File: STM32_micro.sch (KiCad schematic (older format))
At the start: 61 parts

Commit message: asignacion pines de control
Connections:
- net labels added: FMC_A0, FMC_A1, FMC_A2, FMC_A3, FMC_A4, FMC_A5, FMC_A6, FMC_A7, FMC_A[7...0], FMC_D0, FMC_D1, FMC_D10, FMC_D11, FMC_D12, FMC_D13, FMC_D14, FMC_D15, FMC_D2, FMC_D3, FMC_D4, FMC_D5, FMC_D6, FMC_D7, FMC_D8, FMC_D9, FMC_D[15...0], FMC_N_DOUT, JNRST, JTCK, JTDI_FPGA, JTDO, JTMS, JTRST, STM_TCK, STM_TDI, STM_TDO, STM_TMS, STM_TRST
- wire segments 339 -> 389
- no-connect marks 4 -> 2

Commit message: asignacion pines de control
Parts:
- removed J?: Conn_02x05_Odd_Even, symbol Connector_Generic:Conn_02x05_Odd_Even
- removed R? (x15): 39, symbol BAT2032:R
- added J3: Conn_02x06_Odd_Even, symbol Connector_Generic:Conn_02x06_Odd_Even
- Y1: renamed from Y?; footprint CRYSTAL_ABM8G -> library:GSG-XTAL3.2x2.5mm; digikey (none) -> 535-10289-1-ND
- gave numbers to parts that had none: 44
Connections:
- net labels added: +5V, adCLK, adCS, adCSK, adMOSI
- net labels removed: FPGA_B_1, FPGA_B_10, FPGA_B_11, FPGA_B_12, FPGA_B_13, FPGA_B_14, FPGA_B_15, FPGA_B_2, FPGA_B_3, FPGA_B_4, FPGA_B_5, FPGA_B_6, FPGA_B_7, FPGA_B_8, FPGA_B_9, P_FPGA_2, P_FPGA_3, P_FPGA_4, P_FPGA_5, P_FPGA_6, P_FPGA_7, P_FPGA_8, P_FPGA_9
- wire segments 389 -> 355
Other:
- note added: "ACELEROMETRO, GIROSCOPIO IMU"

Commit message: retoque casi finales
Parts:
- removed J4: Conn_01x16_Male, symbol Connector:Conn_01x16_Male
- added D12, D13: LED, LED_SMD:LED_0603_1608Metric_Pad1.05x0.95mm_HandSolder, symbol BAT2032:LED
- added J4: Conn_02x10_Odd_Even, Connector_PinHeader_2.54mm:PinHeader_2x10_P2.54mm_Vertical, symbol Connector_Generic:Conn_02x10_Odd_Even
- added R15, R16: 600, Resistor_SMD:R_0603_1608Metric_Pad1.05x0.95mm_HandSolder, symbol BAT2032:R
- R6: footprint (none) -> Resistor_SMD:R_0603_1608Metric_Pad1.05x0.95mm_HandSolder
- U6: digikey (none) -> 497-14946-1-ND
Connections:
- net labels added: !VAA_ENABLE, FMC_A[0..7], FMC_D[0..15], FMC_NE1, FMC_NWAIT, FMC_NWE, FMC_[0..7], GPIO_00, GPIO_01, GPIO_02, GPIO_03, GPIO_04, GPIO_05, GPIO_06, GPIO_07, GPIO_08, GPIO_09, GPIO_10, GPIO_11, GPIO_12, GPIO_13, GPIO_14, GPIO_15, GPIO_CLK, GPIO_INTR, I2C_0[0..1], JTAG[0..5], LED1, LED2, MCU_CLK, SPI1[1..6], SPI1_CS_AD, SPI1_CS_RF, SPI1_RSSI, USART_[0..1], rf_!SHDN, rf_ANTSEL, rf_LD, rf_RSSI, rf_RXHP, rf_RXTX
- net labels removed: AQUI_ENABLE, CS_AD, FMC_A[7...0], FMC_CONTROL, FMC_D[15...0], I2C_0[1..0], JTAG[5...0], MEN_WE, PF0, PF1, PF10, PF11, PF2, PF3, PF4, PF5, PF6, PF7, PF8, PF9, PROC_MAX2837[7.0], PROC_MAX5864, P_FPGA_1, RSSI, RX_ENABLE, TX_ENABLE, adCLK, adCS, adCSK, adMOSI
- wire segments 355 -> 388
- no-connect marks 2 -> 30
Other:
- note added: "BLUE"
- note added: "GREEN"
- note added: "REVISAR ESTAS DOS CONEC"

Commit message: diseño de esquematico
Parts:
- removed R6: R, Resistor_SMD:R_0603_1608Metric_Pad1.05x0.95mm_HandSolder, symbol Device:R
- removed R7, R8: 0, Resistor_SMD:R_0603_1608Metric_Pad1.05x0.95mm_HandSolder, symbol Device:R
- BT1: footprint (none) -> library:MPD_BK-870
- J3: footprint (none) -> Connector_PinHeader_2.54mm:PinHeader_2x06_P2.54mm_Vertical
- L3: renamed from L4; value L -> bead, 600R, 350 mA
- U4: footprint SWITCH_FSM1LPA -> library:FSM1LPTR
- Y2: footprint modules:NX3215SA -> library:NX3215SA
- renumbered C10 to C12, C11 to C13, C12 to C14, C13 to C15, C14 to C16, C15 to C17, C16 to C18, C17 to C19, C18 to C20, C19 to C21, C20 to C22, C21 to C23, C22 to C24, C23 to C25, C24 to C26, C25 to C27, C26 to C28, C27 to C29, C28 to C30, C29 to C31, C30 to C32, C31 to C33, C32 to C34, C33 to C35, C34 to C36, C35 to C37, C36 to C38, C37 to C39, C38 to C40, C39 to C41, C40 to C42, C41 to C43, D12 to D6, D13 to D7, R4 to R5, R15 to R6, R16 to R7, R5 to R8
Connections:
- net labels added: FPGA_JTDO, VCC_5V
- net labels removed: FMC_A[0..7], FMC_D[0..15], FMC_[0..7], I2C_00, I2C_01, I2C_0[0..1], JTAG0, JTAG1, JTAG2, JTAG3, JTAG4, JTAG5, JTAG[0..5], JTDI_FPGA, P_FPGA_10, P_FPGA_11, P_FPGA_12, P_FPGA_13, P_FPGA_14, P_FPGA_15, SPI1[1..6], SPI1_NSS, TCK, TDI, TDO, TMS, TRST, USART_[0..1]
- wire segments 388 -> 370
- no-connect marks 30 -> 36

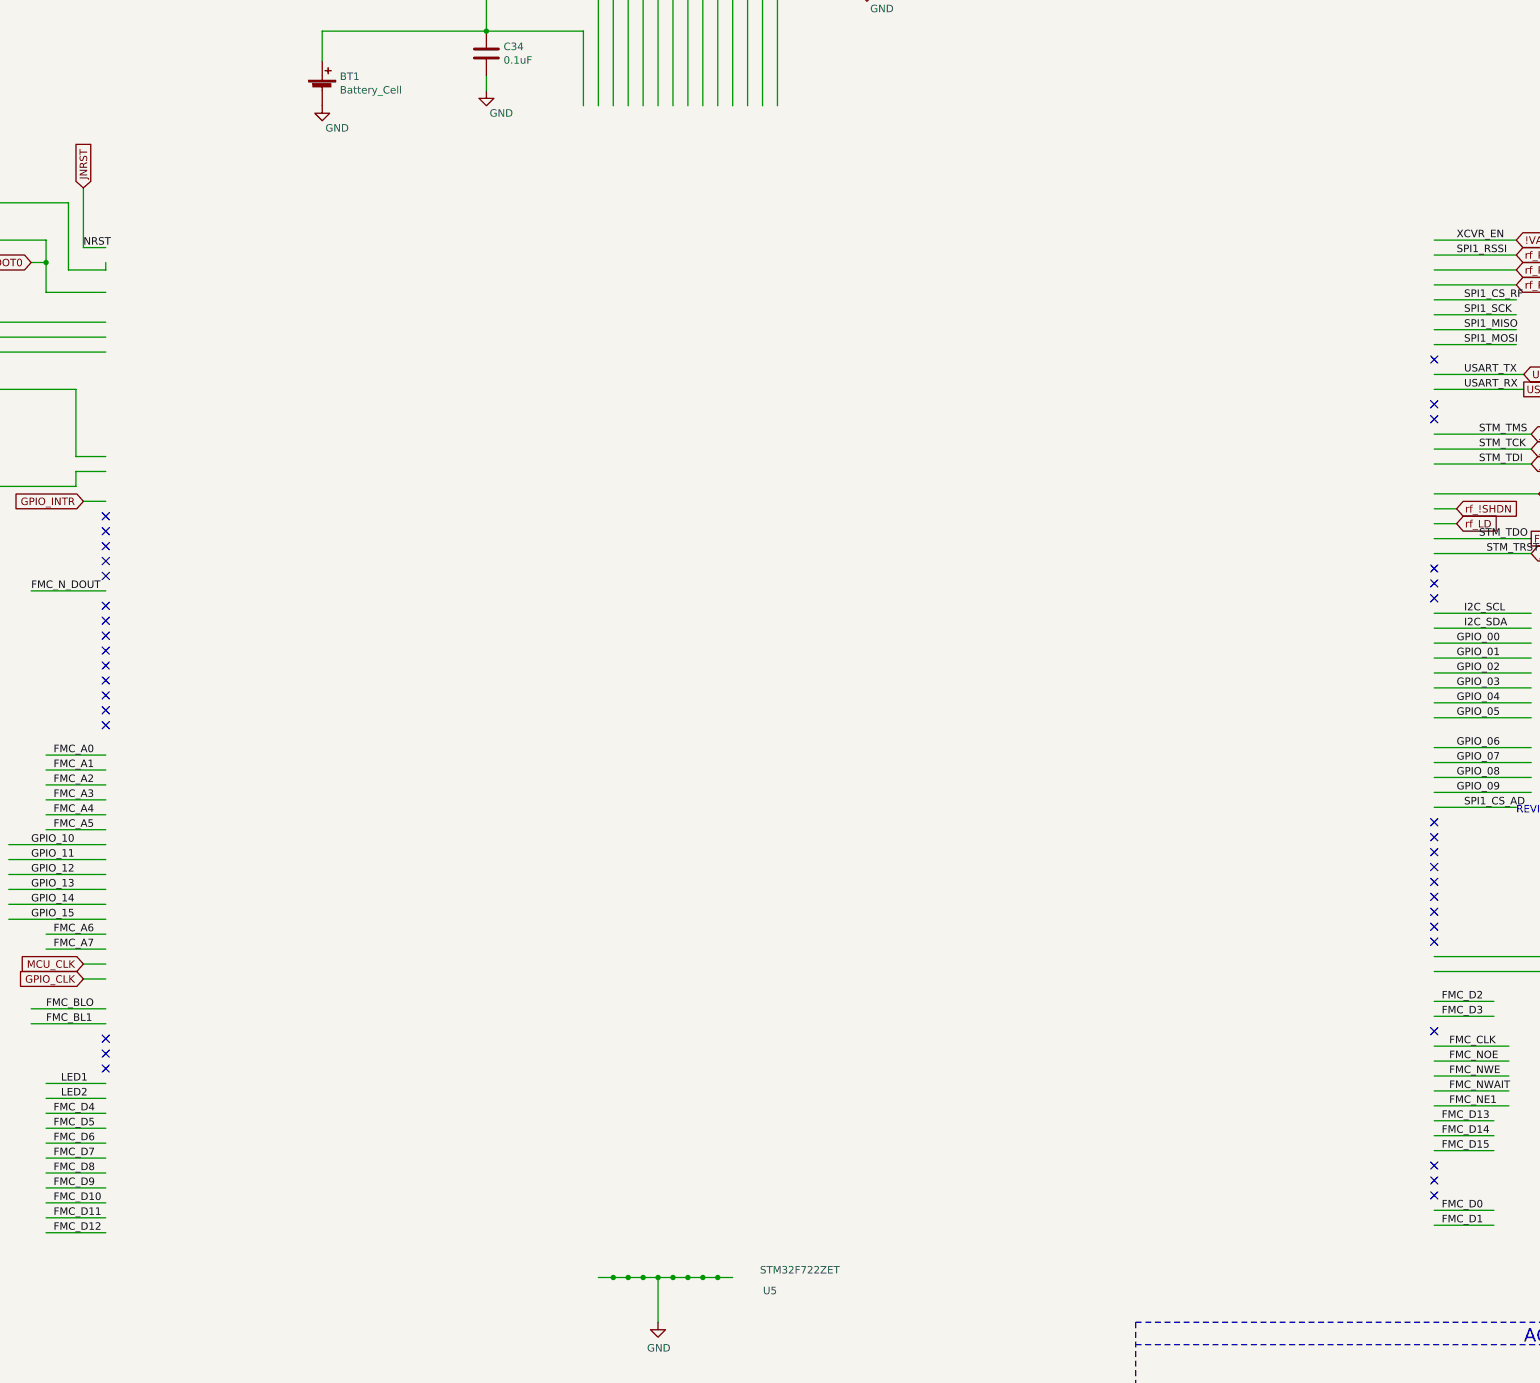
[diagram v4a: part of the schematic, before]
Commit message: diseño de esquematico fm
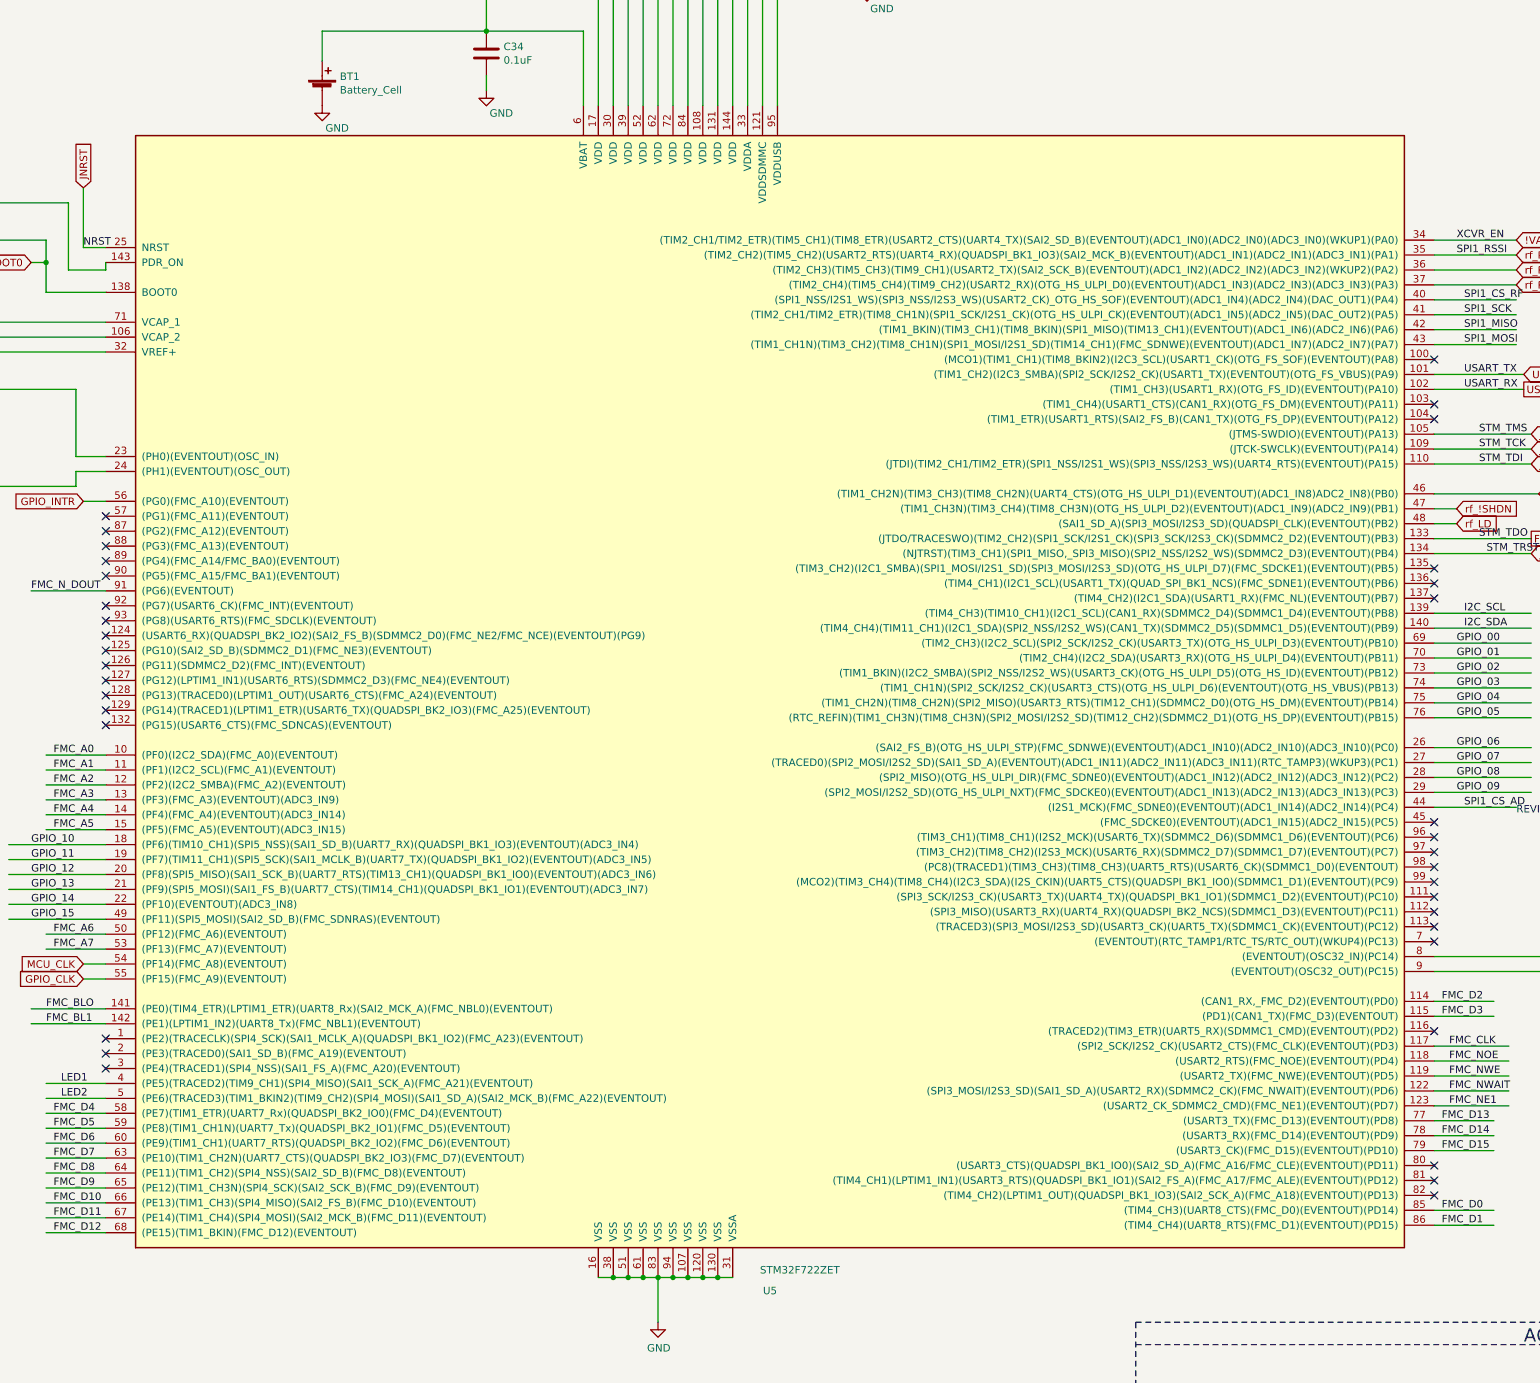
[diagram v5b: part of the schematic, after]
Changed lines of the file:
@@
 $Comp
 L power-rescue:STM32F722ZET-stm32f722zet2 U?
-U 0 0 5D60F773
+U 1 1 5D60F773
 P 8350 4700
 AR Path="/5D60F773" Ref="U?"  Part="1"
-AR Path="/5CD05F2F/5D60F773" Ref="U5"  Part="0"
+AR Path="/5CD05F2F/5D60F773" Ref="U5"  Part="1"
 F 0 "U5" H 11900 -1339 50  0000 C CNN
 F 1 "STM32F722ZET" H 12100 -1200 50  0000 C CNN
@@
 F 3 "" H 7550 6650 50  0001 C CNN
 F 4 "497-18558-ND" H 8350 4700 50  0001 C CNN "digikey"
-	0    8350 4700
+	1    8350 4700
 	1    0    0    -1
 $EndComp

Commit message: diseño de esquematico CASI FINAL
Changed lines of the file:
@@
-EESchema Schematic File Version 4
+EESchema Schematic File Version 5
 LIBS:power-cache
 EELAYER 29 0
@@
 Wire Wire Line
 	16350 6300 17000 6300
-Text Label 16550 6300 0    50   ~ 0
-I2C_SDA
 Text Label 16550 6200 0    50   ~ 0
 I2C_SCL
@@
 	16350 3800 16900 3800
 Wire Wire Line
-	16350 3900 16900 3900
-Wire Wire Line
 	16350 4000 16900 4000
-Wire Wire Line
-	16350 3700 16900 3700
-Text Label 16500 3700 0    50   ~ 0
-XCVR_EN
-Text Label 16500 3800 0    50   ~ 0
-SPI1_RSSI
 Wire Wire Line
 	16350 7500 16900 7500
@@
 Text Label 20450 12400 2    50   ~ 0
 INT2_A_G
-Text Label 20450 12500 2    50   ~ 0
+Text Label 19150 12400 2    50   ~ 0
 INT1_A_G
 Wire Wire Line
@@
 Wire Wire Line
 	19900 12700 20550 12700
-Text Label 20450 12600 2    50   ~ 0
+Text Label 20400 12700 2    50   ~ 0
 SDO_A_G
-Text Label 20450 12700 2    50   ~ 0
+Text Label 20400 12600 2    50   ~ 0
 CS_A_G
 Wire Wire Line
@@
 Wire Wire Line
 	19400 12400 18800 12400
-Text Label 19100 12700 2    50   ~ 0
+Text Label 19150 12600 2    50   ~ 0
 CS_M
-Text Label 19100 12600 2    50   ~ 0
+Text Label 19150 12700 2    50   ~ 0
 SDO_M
+Text Label 20400 12500 2    50   ~ 0
+DRDY_M
 Text Label 19100 12500 2    50   ~ 0
-DRDY_M
-Text Label 19100 12400 2    50   ~ 0
 INT_M
 Wire Wire Line
@@
 Text Notes 16900 7550 0    50   ~ 0
 REVISAR ESTAS DOS CONEC
-Text GLabel 16900 3700 2    50   Input ~ 0
-!VAA_ENABLE
 Text GLabel 16900 3800 2    50   Input ~ 0
-rf_RSSI
-Text GLabel 16900 3900 2    50   Input ~ 0
 rf_RXHP
 Text GLabel 16900 4000 2    50   Input ~ 0
@@
 NoConn ~ 16350 4900
 Wire Wire Line
-	16350 6400 17000 6400
-Text Label 16500 6400 0    50   ~ 0
-GPIO_00
-Wire Wire Line
-	16350 6500 17000 6500
-Text Label 16500 6500 0    50   ~ 0
-GPIO_01
-Wire Wire Line
-	16350 6600 17000 6600
-Text Label 16500 6600 0    50   ~ 0
+	18900 4400 19550 4400
+Wire Wire Line
+	18900 4500 19550 4500
+Text Label 19100 4500 0    50   ~ 0
 GPIO_02
-Wire Wire Line
-	16350 6700 17000 6700
-Text Label 16500 6700 0    50   ~ 0
-GPIO_03
-Wire Wire Line
-	16350 6800 17000 6800
-Text Label 16500 6800 0    50   ~ 0
+Text Label 19100 4600 0    50   ~ 0
 GPIO_04
 Wire Wire Line
-	16350 6900 17000 6900
-Text Label 16500 6900 0    50   ~ 0
-GPIO_05
-Wire Wire Line
-	18900 4400 19550 4400
-Text Label 19050 4400 0    50   ~ 0
-GPIO_00
-Wire Wire Line
-	18900 4500 19550 4500
-Text Label 19050 4500 0    50   ~ 0
-GPIO_01
-Wire Wire Line
-	18900 4600 19550 4600
-Text Label 19050 4600 0    50   ~ 0
-GPIO_02
-Wire Wire Line
 	18900 4700 19550 4700
-Text Label 19050 4700 0    50   ~ 0
-GPIO_03
+Text Label 19100 4700 0    50   ~ 0
+GPIO_06
 Wire Wire Line
 	18900 4800 19550 4800
-Text Label 19050 4800 0    50   ~ 0
-GPIO_04
+Text Label 19100 4800 0    50   ~ 0
+GPIO_08
 Wire Wire Line
 	18900 4900 19550 4900
-Text Label 19050 4900 0    50   ~ 0
-GPIO_05
-Wire Wire Line
-	16350 7100 17000 7100
-Text Label 16500 7100 0    50   ~ 0
-GPIO_06
+Text Label 19100 4900 0    50   ~ 0
+GPIO_10
+Wire Wire Line
+	16350 7400 17000 7400
+Wire Wire Line
+	16350 7300 17000 7300
 Wire Wire Line
 	16350 7200 17000 7200
-Text Label 16500 7200 0    50   ~ 0
-GPIO_07
-Wire Wire Line
-	16350 7300 17000 7300
-Text Label 16500 7300 0    50   ~ 0
-GPIO_08
-Wire Wire Line
-	16350 7400 17000 7400
-Text Label 16500 7400 0    50   ~ 0
-GPIO_09
 Wire Wire Line
 	6800 7750 7450 7750
-Text Label 6950 7750 0    50   ~ 0
-GPIO_10
 Wire Wire Line
 	6800 7850 7450 7850
-Text Label 6950 7850 0    50   ~ 0
+Text Label 7350 8150 2    50   ~ 0
 GPIO_11
 Wire Wire Line
 	6800 7950 7450 7950
-Text Label 6950 7950 0    50   ~ 0
+Text Label 7350 8050 2    50   ~ 0
 GPIO_12
 Wire Wire Line
 	6800 8050 7450 8050
-Text Label 6950 8050 0    50   ~ 0
+Text Label 7350 7950 2    50   ~ 0
 GPIO_13
 Wire Wire Line
 	6800 8150 7450 8150
-Text Label 6950 8150 0    50   ~ 0
+Text Label 7350 7850 2    50   ~ 0
 GPIO_14
 Wire Wire Line
 	6800 8250 7450 8250
-Text Label 6950 8250 0    50   ~ 0
+Text Label 7350 7750 2    50   ~ 0
 GPIO_15
 Wire Wire Line
-	20050 4600 20700 4600
-Text Label 20200 4600 0    50   ~ 0
-GPIO_10
-Wire Wire Line
-	20050 4700 20700 4700
-Text Label 20200 4700 0    50   ~ 0
-GPIO_11
-Wire Wire Line
-	20050 4800 20700 4800
-Text Label 20200 4800 0    50   ~ 0
-GPIO_12
-Wire Wire Line
-	20050 4900 20700 4900
-Text Label 20200 4900 0    50   ~ 0
-GPIO_13
-Wire Wire Line
-	20050 5000 20700 5000
-Text Label 20200 5000 0    50   ~ 0
+	18900 5000 19550 5000
+Wire Wire Line
+	18900 5100 19550 5100
+Text Label 19100 5100 0    50   ~ 0
 GPIO_14
-Wire Wire Line
-	20050 5100 20700 5100
-Text Label 20200 5100 0    50   ~ 0
-GPIO_15
-Wire Wire Line
-	20050 4400 20700 4400
-Text Label 20200 4400 0    50   ~ 0
-GPIO_08
-Wire Wire Line
-	20050 4500 20700 4500
-Text Label 20200 4500 0    50   ~ 0
-GPIO_09
-Wire Wire Line
-	18900 5000 19550 5000
-Text Label 19050 5000 0    50   ~ 0
-GPIO_06
-Wire Wire Line
-	18900 5100 19550 5100
-Text Label 19050 5100 0    50   ~ 0
-GPIO_07
 NoConn ~ 16350 5900
 NoConn ~ 16350 6000
@@
 NoConn ~ 16350 10000
 NoConn ~ 16350 10100
-NoConn ~ 7450 9250
-NoConn ~ 7450 9150
 NoConn ~ 7450 9050
+NoConn ~ 7450 9450
+NoConn ~ 7450 9350
 NoConn ~ 7450 6950
 NoConn ~ 7450 6250
 NoConn ~ 7450 6150
-Wire Wire Line
-	7450 9350 7050 9350
-Wire Wire Line
-	7450 9450 7050 9450
-Text Label 7150 9350 0    50   ~ 0
-LED1
-Text Label 7150 9450 0    50   ~ 0
-LED2
 NoConn ~ 7450 5650
 NoConn ~ 7450 5750
@@
 Wire Wire Line
 	19350 12800 19400 12800
+Wire Wire Line
+	7450 9150 7050 9150
+Text Label 7150 9150 0    50   ~ 0
+LED1
+Wire Wire Line
+	7450 9250 7050 9250
+Text GLabel 16900 3900 2    50   Input ~ 0
+rf_RSSI
+Text GLabel 16900 3700 2    50   Input ~ 0
+!VAA_ENABLE
+Text Label 16500 3900 0    50   ~ 0
+SPI1_RSSI
+Text Label 16500 3700 0    50   ~ 0
+XCVR_EN
+Wire Wire Line
+	16350 3700 16900 3700
+Wire Wire Line
+	16350 3900 16900 3900
+Text Label 7150 9250 0    50   ~ 0
+LED2
+Text Label 19100 4400 0    50   ~ 0
+GPIO_00
+Text Label 19100 5000 0    50   ~ 0
+GPIO_12
+Text Label 20200 4500 0    50   ~ 0
+GPIO_03
+Wire Wire Line
+	20050 4500 20700 4500
+Text Label 20200 4400 0    50   ~ 0
+GPIO_01
+Wire Wire Line
+	20050 4400 20700 4400
+Text Label 20200 5100 0    50   ~ 0
+GPIO_15
+Wire Wire Line
+	20050 5100 20700 5100
+Text Label 20200 5000 0    50   ~ 0
+GPIO_13
+Wire Wire Line
+	20050 5000 20700 5000
+Text Label 20200 4900 0    50   ~ 0
+GPIO_11
+Wire Wire Line
+	20050 4900 20700 4900
+Text Label 20200 4800 0    50   ~ 0
+GPIO_09
+Wire Wire Line
+	20050 4800 20700 4800
+Text Label 20200 4700 0    50   ~ 0
+GPIO_07
+Wire Wire Line
+	20050 4700 20700 4700
+Text Label 20200 4600 0    50   ~ 0
+GPIO_05
+Wire Wire Line
+	20050 4600 20700 4600
+Wire Wire Line
+	18900 4600 19550 4600
+Text Label 7050 8250 0    50   ~ 0
+GPIO_06
+Text Label 16700 7100 2    50   ~ 0
+GPIO_10
+Text Label 16500 7200 0    50   ~ 0
+GPIO_09
+Text Label 16500 7300 0    50   ~ 0
+GPIO_08
+Text Label 16500 7400 0    50   ~ 0
+GPIO_07
+Text Label 16550 6300 0    50   ~ 0
+I2C_SDA
+Wire Wire Line
+	16350 6600 17000 6600
+Text Label 16500 6600 0    50   ~ 0
+GPIO_02
+Wire Wire Line
+	16350 6700 17000 6700
+Text Label 16500 6700 0    50   ~ 0
+GPIO_03
+Wire Wire Line
+	16350 6400 17000 6400
+Text Label 16500 6400 0    50   ~ 0
+GPIO_04
+Wire Wire Line
+	16350 6500 17000 6500
+Text Label 16500 6500 0    50   ~ 0
+GPIO_05
+Text Label 16500 6900 0    50   ~ 0
+GPIO_01
+Wire Wire Line
+	16350 6900 17000 6900
+Text Label 16500 6800 0    50   ~ 0
+GPIO_00
+Wire Wire Line
+	16350 6800 17000 6800
+Wire Wire Line
+	16350 7100 17000 7100
 $EndSCHEMATC
